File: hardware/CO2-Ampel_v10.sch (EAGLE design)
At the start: 69 parts, among them IC1 VREG-AP2111H-3V3, IC2 ATSAMD21G18A-MU, IC3 ATWINC1500-MR210PB, IC33 IN-S63DTLS, IC34 SCD30, IC7 ATECC608A-MAHDA, J1 USB-C-S, J2 JST4, J5 JST4, SW1 PTS645SH50SMTR92-Grey, SW2 PTS645SK50SMTR92-Red, T1 N-Chn, X1 PASSER-07, X2 PASSER-07, X3 PASSER-07, X4 PASSER-07

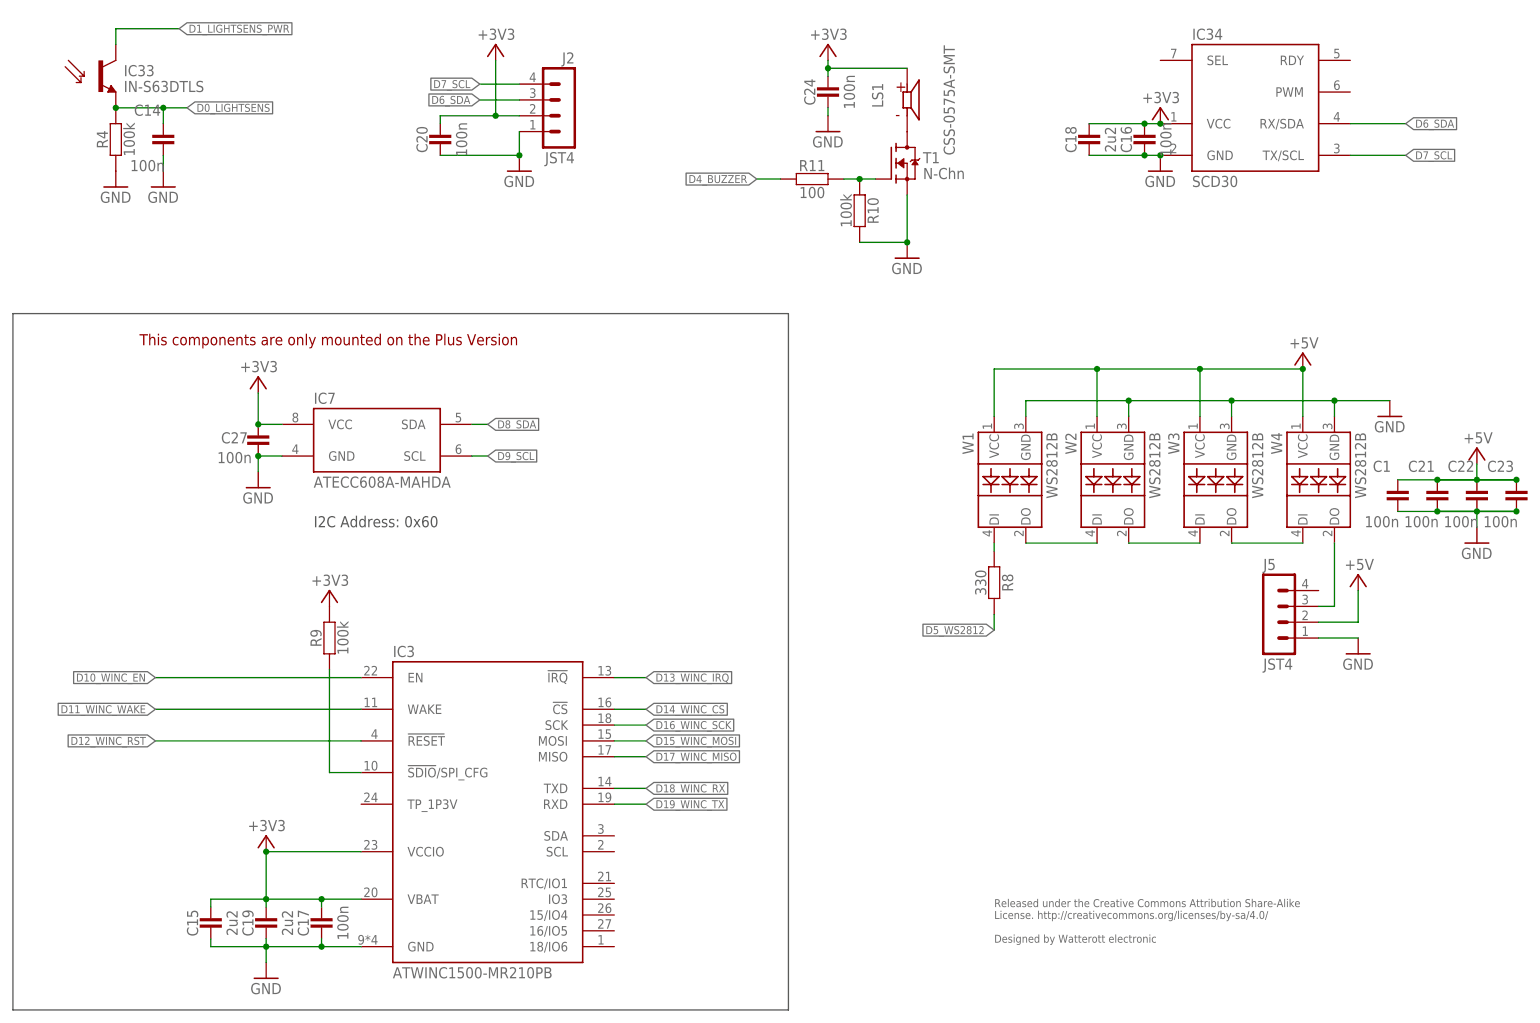
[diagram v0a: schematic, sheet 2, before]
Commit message: updated schematics
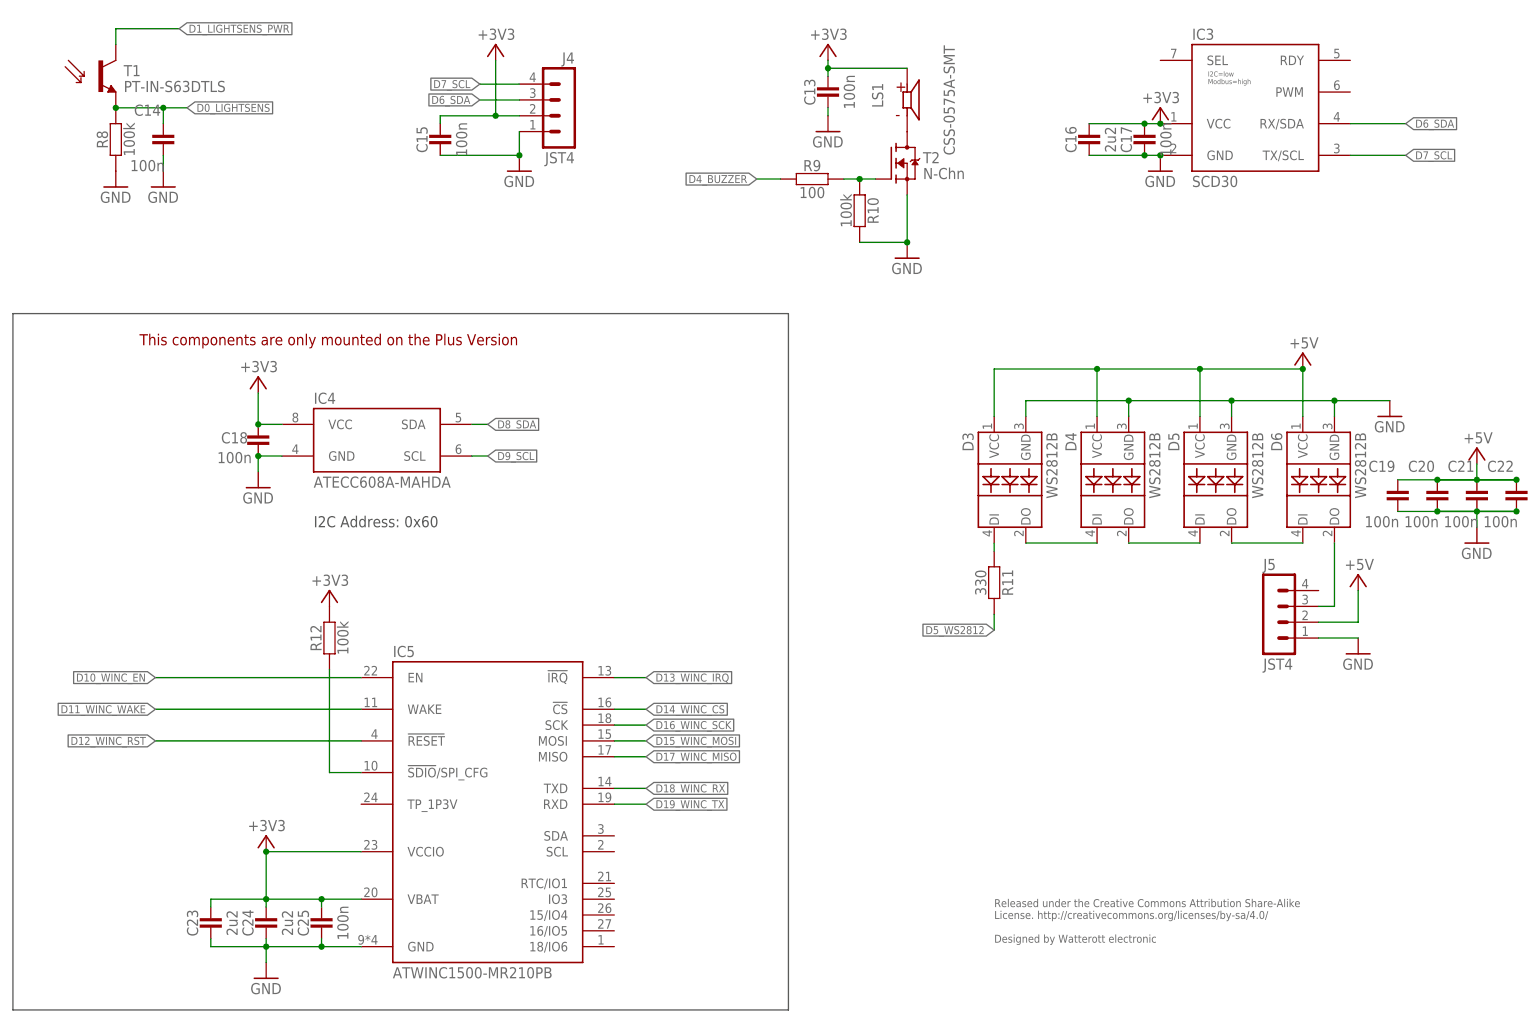
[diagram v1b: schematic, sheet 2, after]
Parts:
- removed C27: 100n, we-rcl:CAPACITOR-0402
- removed IC33: IN-S63DTLS, we-sensor:IN-S63DTLS
- removed IC34: SCD30, we-sensor:SCD30
- removed LOGO7: LOGO_CE-4, we-symbol:LOGO_CE-4
- removed R46, R47: 5k1, we-rcl:RESISTOR-0402
- removed SWD: SWD-2X5-SMD, we-board:SWD-2X5-SMD
- removed W3: WS2812B, we-opto:WS2812B
- added C25: 100n, we-rcl:CAPACITOR-0402
- added D1: D_ESD5V3U2U-03F, we-rcl:D_ESD5V3U2U-03F
- added IC5: ATWINC1500-MR210PB, we-chip:ATWINC1500-MR210PB
- added J4: JST4, we-con:JST4
- added LOGO1: LOGO_SPARK-4, we-symbol:LOGO_SPARK-4
- added R12: 100k, we-rcl:RESISTOR-0402
- added R2: 330, we-rcl:RESISTOR-0402
- added T2: N-Chn, we-transistor:MOSFET-N-SOT23
- C10, C13, C15, C18, C19: value 2u2 -> 100n
- C12: value 100n -> 22u; device we-rcl:CAPACITOR-0402 -> we-rcl:CAPACITOR-0805
- C16, C23, C24, C5, C6: value 100n -> 2u2
- C2: value 22u -> 100n; device we-rcl:CAPACITOR-0805 -> we-rcl:CAPACITOR-0402
- D5: value D_ESD5V3U2U-03F -> WS2812B; device we-rcl:D_ESD5V3U2U-03F -> we-opto:WS2812B
- IC1: value VREG-AP2111H-3V3 -> ATSAMD21G18A-MU; device we-power:VREG-TS1117CW-3V3 -> we-chip:ATSAMD21G18A-MU
- IC2: value ATSAMD21G18A-MU -> VREG-AP2111H-3V3; device we-chip:ATSAMD21G18A-MU -> we-power:VREG-TS1117CW-3V3
- IC3: value ATWINC1500-MR210PB -> SCD30; device we-chip:ATWINC1500-MR210PB -> we-sensor:SCD30
- J2: value JST4 -> SWD-2X5-SMD; device we-con:JST4 -> we-board:SWD-2X5-SMD
- LOGO4: value LOGO_SPARK-4 -> LOGO_ROHS-4; device we-symbol:LOGO_SPARK-4 -> we-symbol:LOGO_ROHS-4
- LOGO5: value LOGO_ROHS-4 -> LOGO_CE-4; device we-symbol:LOGO_ROHS-4 -> we-symbol:LOGO_CE-4
- R1: value 0 -> 10k; device we-rcl:RESISTOR-0603 -> we-rcl:RESISTOR-0402
- R11: value 100 -> 330
- R3: value 1k -> 5k1
- R4: value 100k -> 5k1
- R5: value 1k -> 0; device we-rcl:RESISTOR-0402 -> we-rcl:RESISTOR-0603
- R6: value 330 -> 1k
- R7: value 10k -> 1k
- R8: value 330 -> 100k
- R9: value 100k -> 100
- SW1: value PTS645SH50SMTR92-Grey -> PTS645SK50SMTR92-Red
- SW2: value PTS645SK50SMTR92-Red -> PTS645SH50SMTR92-Grey
- T1: value N-Chn -> PT-IN-S63DTLS; device we-transistor:MOSFET-N-SOT23 -> we-opto@1:PT-IN-S63DTLS
- renumbered IC7 to IC4, LOGO6 to LOGO2, SWD_TP to J3, W1 to D3, W2 to D4, W4 to D6
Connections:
- net +3V3: now also C11.2, C12.2, C13.2, C2.2, C23.2, C25.2, C3.2, IC1.VCCIN, IC1.VCCIO, IC2.VOUT, IC3.VCC, IC5.VBAT, IC5.VCCIO, J2.VCC, J4.2, R1.1, R12.2, R6.1; no longer C19.2, C20.2, C27.2, C5.2, C6.2, C7.2, C9.2, IC1.VOUT, IC2.VCCIN, IC2.VCCIO, IC3.VBAT, IC3.VCCIO, IC34.VCC, J2.2, R5.1, R7.1, R9.2, SWD.VCC
- net +5V: now also C10.2, C19.2, C20.2, C9.2, D5.VCC, IC2.VIN; no longer C1.2, C2.2, C23.2, C3.2, IC1.VIN, W3.VCC
- net CC1: now also R4.1; no longer R46.1
- net CC2: now also R3.1; no longer R47.1
- net CFG: now also IC5.!SDIO!/SPI_CFG, R12.1; no longer IC3.!SDIO!/SPI_CFG, R9.1
- net D0_LIGHTSENS: now also IC1.(DAC/AIN0)PA02, R8.2, T1.E; no longer IC2.(DAC/AIN0)PA02, IC33.E, R4.2
- net D10_WINC_EN: now also IC1.(S4:2/T5:0|0:4)PB10, IC5.EN; no longer IC2.(S4:2/T5:0|0:4)PB10, IC3.EN
- net D11_WINC_WAKE: now also IC1.(S4:3/T5:1|0:5)PB11, IC5.WAKE; no longer IC2.(S4:3/T5:1|0:5)PB11, IC3.WAKE
- net D12_WINC_RST: now also IC1.(S0:2|2:2/T1:0|0:2/AIN18)PA10, IC5.!RESET; no longer IC2.(S0:2|2:2/T1:0|0:2/AIN18)PA10, IC3.!RESET
- net D13_WINC_IRQ: now also IC1.(S5:2|3:2/T7:0|0:6)PA20, IC5.!IRQ; no longer IC2.(S5:2|3:2/T7:0|0:6)PA20, IC3.!IRQ
- net D14_WINC_CS: now also IC1.(S1:2|3:2/T3:0|0:2)PA18, IC5.!CS; no longer IC2.(S1:2|3:2/T3:0|0:2)PA18, IC3.!CS
- net D15_WINC_MOSI: now also IC1.(SDA/S1:0|3:0/T2:0|0:6)PA16, IC5.MOSI; no longer IC2.(SDA/S1:0|3:0/T2:0|0:6)PA16, IC3.MOSI
- net D16_WINC_SCK: now also IC1.(SCL/S1:1|3:1/T2:1|0:7)PA17, IC5.SCK; no longer IC2.(SCL/S1:1|3:1/T2:1|0:7)PA17, IC3.SCK
- net D17_WINC_MISO: now also IC1.(S1:3|3:3/T3:1|0:3)PA19, IC5.MISO; no longer IC2.(S1:3|3:3/T3:1|0:3)PA19, IC3.MISO
- net D18_WINC_RX: now also IC1.(S5:3/T7:1)PB23, IC5.TXD; no longer IC2.(S5:3/T7:1)PB23, IC3.TXD
- net D19_WINC_TX: now also IC1.(S5:2/T7:0)PB22, IC5.RXD; no longer IC2.(S5:2/T7:0)PB22, IC3.RXD
- net D1_LIGHTSENS_PWR: now also IC1.(REFA/AIN1)PA03, T1.C; no longer IC2.(REFA/AIN1)PA03, IC33.C
- net D2_SWITCH: now also IC1.(S:1/T6:1/AIN11)PB03, SW2.P1; no longer IC2.(S:1/T6:1/AIN11)PB03, SW1.P1
- net D3_STATUSLED: now also IC1.PA27, R7.1; no longer IC2.PA27, R3.1
- net D4_BUZZER: now also IC1.(S0:1/T0:1/AIN5)PA05, R9.1; no longer IC2.(S0:1/T0:1/AIN5)PA05, R11.1
- net D5_WS2812: now also IC1.(SDA/S3:0|5:0/T4:0|0:4)PA22, R11.2; no longer IC2.(SDA/S3:0|5:0/T4:0|0:4)PA22, R8.2
- net D6_SDA: now also IC1.(SDA/S0:0|2:0/T0:0|1:2/AIN16)PA08, IC3.RX/SDA, J4.3; no longer IC2.(SDA/S0:0|2:0/T0:0|1:2/AIN16)PA08, IC34.RX/SDA, J2.3
- net D7_SCL: now also IC1.(SCL/S0:1|2:1/T0:1|1:3/AIN17)PA09, IC3.TX/SCL, J4.4; no longer IC2.(SCL/S0:1|2:1/T0:1|1:3/AIN17)PA09, IC34.TX/SCL, J2.4
- net D8_SDA: now also IC1.(SDA/S2:0|4:0/T2:0|0:6)PA12; no longer IC2.(SDA/S2:0|4:0/T2:0|0:6)PA12
- net D9_SCL: now also IC1.(SCL/S2:1|4:1/T2:1|0:7)PA13; no longer IC2.(SCL/S2:1|4:1/T2:1|0:7)PA13
- net GND: now also C25.1, D1.A, D5.GND, IC5.GND, J2.GND, J4.1, R3.2, R4.2, R5.1, R8.1, T2.S; no longer C27.1, D5.A, IC34.GND, J2.1, R1.1, R4.1, R46.2, R47.2, SWD.GND, T1.S, W3.GND
- net N$1: now also T2.D; no longer T1.D
- net N$2: now also R9.2, T2.G; no longer R11.2, T1.G
- net N$3: now also R7.2; no longer R3.2
- net N$4: now also R11.1; no longer R8.1
- net N$8: now also R2.2, SW1.P1; no longer R6.2, SW2.P1
- net RST: now also C1.2, IC1.!RESET, J2.RST, R1.2, R2.1; no longer C12.2, IC2.!RESET, R6.1, R7.2, SWD.RST
- net SHLD: now also R5.2; no longer R1.2
- net SWCLK: now also IC1.(SWCLK/S1:2/T1:0)PA30, J2.SWCLK, R6.2; no longer IC2.(SWCLK/S1:2/T1:0)PA30, R5.2, SWD.SWCLK
- net SWDIO: now also IC1.(SWDIO/S1:3/T1:1)PA31, J2.SWDIO; no longer IC2.(SWDIO/S1:3/T1:1)PA31, SWD.SWDIO
- net USB_N: now also D1.C1, IC1.(USBM/S3:2|5:2/T5:0|1:2)PA24; no longer D5.C1, IC2.(USBM/S3:2|5:2/T5:0|1:2)PA24
- net USB_P: now also D1.C2, IC1.(USBP/S3:3|5:3/T5:1|1:3)PA25; no longer D5.C2, IC2.(USBP/S3:3|5:3/T5:1|1:3)PA25
- net VCCANA: now also C5.2, C6.2, C7.2, IC1.VCCANA; no longer C10.2, C11.2, C8.2, IC2.VCCANA
- net VCCCORE: now also C8.2, IC1.VCCCORE; no longer C13.2, IC2.VCCCORE
- net W2OUT: now also D5.DI; no longer W3.DI
- net W3OUT: now also D5.DO; no longer W3.DO
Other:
- moved on the sheet: C10, C11, C12, C15, C16, C17, C18, C19, C2, C20, C21, C22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
